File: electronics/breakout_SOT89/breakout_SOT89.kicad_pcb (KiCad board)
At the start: 2 copper layers, 4 parts, among them J1 Conn_01x03, U1 Generic_SOT23-3

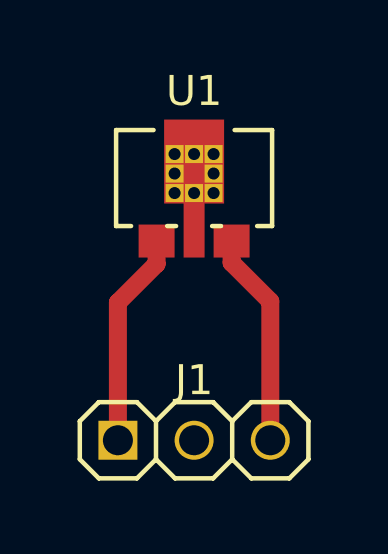
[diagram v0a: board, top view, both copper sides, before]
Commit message: place&route&silk position completed
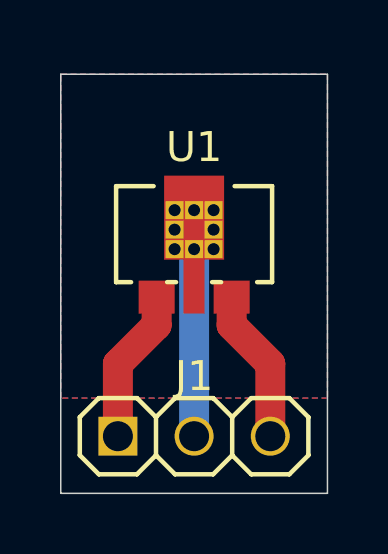
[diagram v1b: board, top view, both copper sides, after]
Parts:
- moved U1 1.87 mm to (151.1, 81.9)
- moved J1 0.14 mm to (151.1, 88.3)
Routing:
- net /2: track 0.00 -> 6.23 mm
- net /3: track 7.17 -> 5.17 mm
- net /1: track 7.17 -> 5.17 mm
- added copper zone on B.Cu, net /2
- added copper zone on F.Cu, net /2
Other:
- board outline added: 8.9 x 14 mm
